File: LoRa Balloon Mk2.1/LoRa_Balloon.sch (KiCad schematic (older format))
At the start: 64 parts, among them J1 Qwiic_4pin, J2 Qwicc_6-pin, U1 SKY67013-396LF_CID141, U2 SX1272IMLTRICT-ND_CID104, U3 SKY67013-396LF_CID141, U4 PE4259_CID105, U5 ATMEGA328P-AU, U6 XCL205, X1 X1E0000210162_CID142, X2 7A-12.000MAAJ-T_CID117

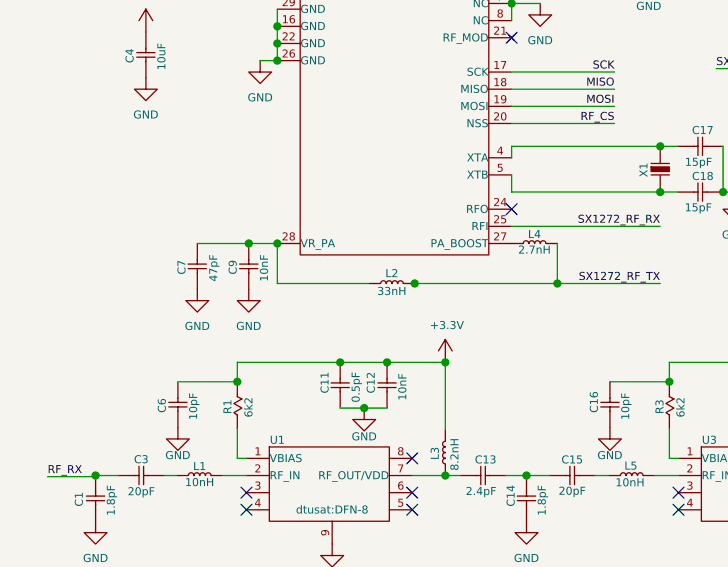
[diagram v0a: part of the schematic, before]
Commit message: Updated libraries
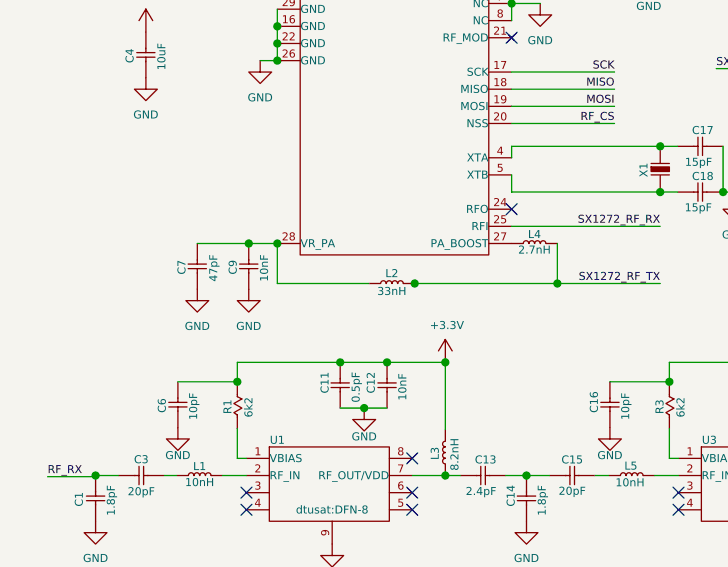
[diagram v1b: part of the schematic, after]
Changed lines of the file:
@@
 EESchema Schematic File Version 4
-LIBS:LoRa_Balloon-cache
 EELAYER 30 0
 EELAYER END
@@
 Wire Wire Line
 	2118 2890 2742 2890
-Wire Wire Line
-	1517 2890 1917 2890
 Text Label 4515 5209 2    35   ~ 0
 Reset
@@
 Text Notes 3813 6511 2    157  ~ 0
 GPS\n
+Wire Wire Line
+	1517 2890 1918 2890
 $EndSCHEMATC
